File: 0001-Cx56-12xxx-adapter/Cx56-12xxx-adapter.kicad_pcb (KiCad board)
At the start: 2 copper layers, 60 x 40 mm, 11 parts, among them J1 Conn_01x08_Pin, J2 Conn_01x04_Pin, U1 CC56-12EWA

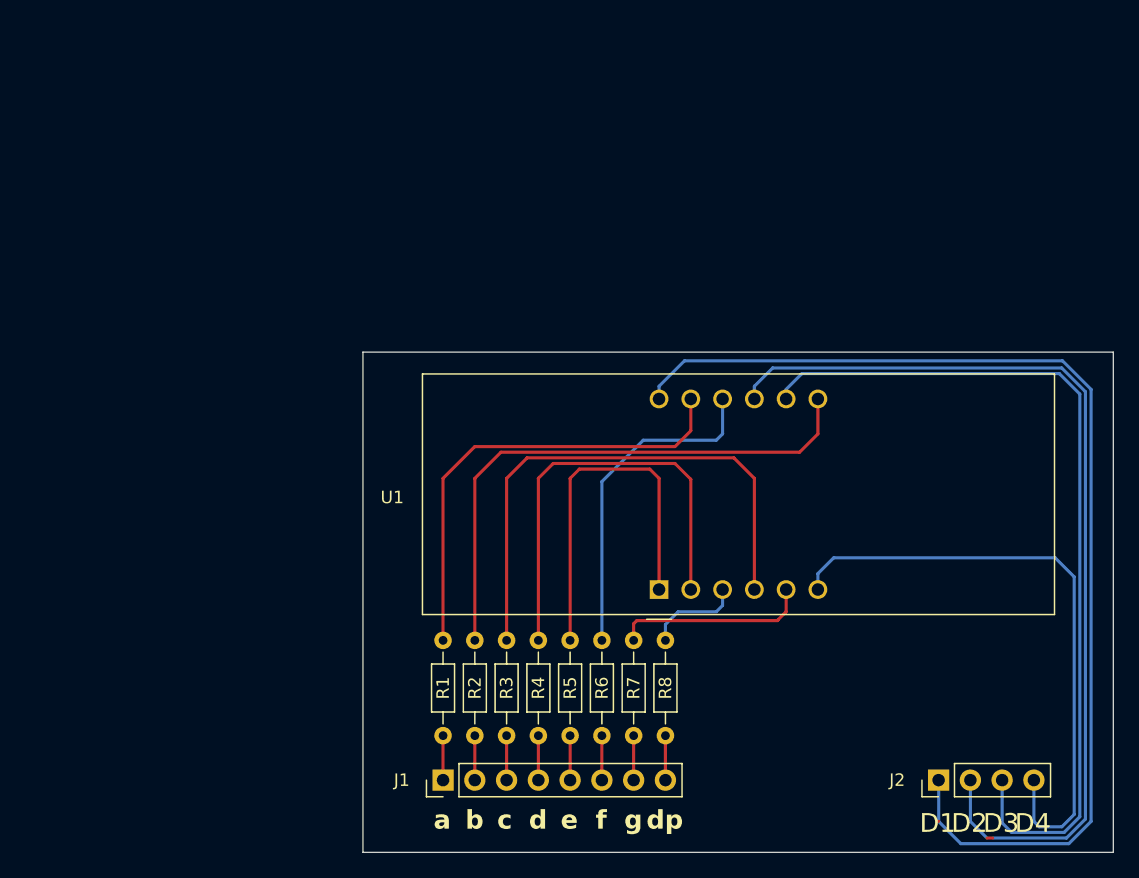
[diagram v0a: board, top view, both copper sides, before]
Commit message: Seven-segment display adapter based on CX-12XXX (adjustment)
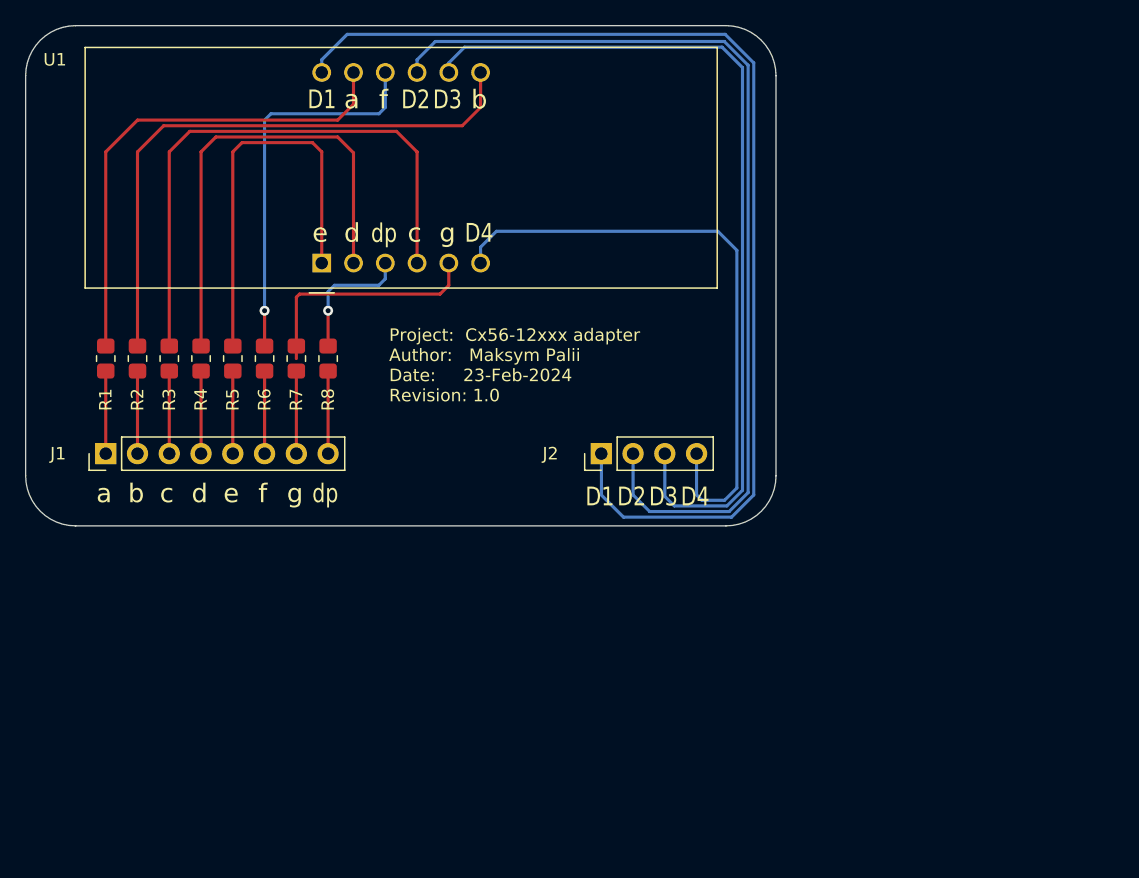
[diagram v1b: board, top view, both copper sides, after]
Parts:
- R1, R2, R3, R4, R5, R6, R7, R8: footprint Resistor_THT:R_Axial_DIN0204_L3.6mm_D1.6mm_P7.62mm_Horizontal -> Resistor_SMD:R_0805_2012Metric_Pad1.20x1.40mm_HandSolder
- moved U1 37.5 mm to (93.7, 59.0)
- moved J2 37.5 mm to (116.0, 74.2)
- moved J1 37.5 mm to (76.4, 74.2)
- moved R2 35.1 mm to (78.9, 66.6)
- moved R4 35.1 mm to (84.0, 66.6)
- moved R6 35.1 mm to (89.1, 66.6)
- moved R1 35.1 mm to (76.4, 66.6)
- moved R3 35.1 mm to (81.5, 66.6)
- moved R5 35.1 mm to (86.6, 66.6)
- moved R7 35.1 mm to (91.6, 66.6)
- moved R8 35.1 mm to (94.2, 66.6)
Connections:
- net Net-(J2-Pin_1) renamed DataD1
- net Net-(J2-Pin_2) renamed DataD2
- net Net-(J2-Pin_3) renamed DataD3
- net Net-(J2-Pin_4) renamed DataD4
- J1 pad 1: /Data0 -> Data0''
- J1 pad 2: /Data1 -> Data1''
- J1 pad 3: /Data2 -> Data2''
- J1 pad 4: /Data3 -> Data3''
- J1 pad 5: /Data4 -> Data4''
- J1 pad 6: /Data5 -> Data5''
- J1 pad 7: /Data6 -> Data6''
- J1 pad 8: /Data7 -> Data7''
- R1 pad 1: /Data0 -> Data0'
- R1 pad 2: /Data0 -> Data0''
- R2 pad 1: /Data1 -> Data1'
- R2 pad 2: /Data1 -> Data1''
- R3 pad 1: /Data2 -> Data2'
- R3 pad 2: /Data2 -> Data2''
- R4 pad 1: /Data3 -> Data3'
- R4 pad 2: /Data3 -> Data3''
- R5 pad 1: /Data4 -> Data4'
- R5 pad 2: /Data4 -> Data4''
- R6 pad 1: /Data5 -> Data5'
- R6 pad 2: /Data5 -> Data5''
- R7 pad 1: /Data6 -> Data6'
- R7 pad 2: /Data6 -> Data6''
- R8 pad 1: /Data7 -> Data7'
- R8 pad 2: /Data7 -> Data7''
- U1 pad 1: /Data4 -> Data4'
- U1 pad 10: /Data5 -> Data5'
- U1 pad 11: /Data0 -> Data0'
- U1 pad 2: /Data3 -> Data3'
- U1 pad 3: /Data7 -> Data7'
- U1 pad 4: /Data2 -> Data2'
- U1 pad 5: /Data6 -> Data6'
- U1 pad 7: /Data1 -> Data1'
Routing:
- net /Data1: track 48.2 -> 0.00 mm
- net Data1': track 0.00 -> 47.2 mm
- net /Data2: track 46.6 -> 0.00 mm
- net Data2': track 0.00 -> 45.6 mm
- net /Data0: track 40.4 -> 0.00 mm
- net Data0': track 0.00 -> 39.5 mm
- net /Data3: track 38.5 -> 0.00 mm
- net Data3': track 0.00 -> 37.5 mm
- net /Data4: track 33.1 -> 0.00 mm
- net Data4': track 0.00 -> 32.1 mm
- net Data5': track 0.00 -> 30.9 mm, vias 0 -> 1
- net /Data5: track 30.3 -> 0.00 mm
- net Data6': track 0.00 -> 19.6 mm
- net /Data6: track 19.3 -> 0.00 mm
- net Data7': track 0.00 -> 13.7 mm, vias 0 -> 1
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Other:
- outline, holes or cut-outs redrawn
- board text added: "Bill of materials J1 - Pin Male Header 2.54mm, 1x8, straight J2 - Pin Male Header 2.54mm, 1x4, straight R1..R8 - SMD 0805 Resistor 300Ω U1 - Cx56-12xxx Four Digit Numeric Display"
- board text added: "Project: Cx56-12xxx adapter Author: Maksym Palii Date: 23-Feb-2024 Revision: 1.0"
